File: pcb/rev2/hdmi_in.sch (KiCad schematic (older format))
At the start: 22 parts, among them CN1 MOLEX_500254-1927, IC8 PRTR5V0U2X, IC9 PRTR5V0U2X, Q1 BSS84LT1G, Q2 2N7002, Q3 2N7002, Q4 2N7002

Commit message: pcb wip
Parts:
- C1, C28: footprint CAPC1608X87N -> Capacitors SMD:CAPC1608X87N
- D10: footprint SOD3715X145N -> ICs And Semiconductors SMD:SOD3715X145N
- IC8, IC9: footprint SOT190P230X110-4N -> ICs And Semiconductors SMD:SOT190P230X110-4N
- Q1: footprint SOT95P240X110-3N -> ICs And Semiconductors SMD:SOT95P240X110-3N
- Q2, Q3, Q4: footprint SOT95P240X130-3N -> ICs And Semiconductors SMD:SOT95P240X130-3N
- R22, R23, R24, R25, R26, R27, R28, R29, R30, R31: footprint RESC1608X55N -> Resistors SMD:RESC1608X55N
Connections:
- wire segments 123 -> 98
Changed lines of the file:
@@
 F 0 "R27" V 1904 3510 50  0000 L CNN
 F 1 "R0603_1M_1%_0.1W_100PPM" H 1800 3240 60  0001 L CNN
-F 2 "RESC1608X55N" H 1800 2430 60  0001 L CNN
+F 2 "Resistors SMD:RESC1608X55N" H 1800 2430 60  0001 L CNN
 F 3 "\\cern.ch\\dfs\\Applications\\Altium\\Datasheets\\R0603_NIC_NRC.pdf" H 1800 3060 60  0001 L CNN
 F 4 "1M" V 1995 3510 50  0000 L CNN "~"
@@
 F 0 "C28" V 1504 3560 50  0000 L CNN
 F 1 "CC0603_100NF_50V_10%_X7R" H 1400 3190 60  0001 L CNN
-F 2 "CAPC1608X87N" H 1400 2380 60  0001 L CNN
+F 2 "Capacitors SMD:CAPC1608X87N" H 1400 2380 60  0001 L CNN
 F 3 "\\cern.ch\\dfs\\Applications\\Altium\\Datasheets\\CC0603_X7R_PHYCOMP.pdf" H 1400 3010 60  0001 L CNN
 F 4 "100nF" V 1595 3560 50  0000 L CNN "~"
@@
 F 0 "R30" V 1604 4610 50  0000 L CNN
 F 1 "R0603_3K3_1%_0.1W_100PPM" H 1500 4340 60  0001 L CNN
-F 2 "RESC1608X55N" H 1500 3530 60  0001 L CNN
+F 2 "Resistors SMD:RESC1608X55N" H 1500 3530 60  0001 L CNN
 F 3 "\\cern.ch\\dfs\\Applications\\Altium\\Datasheets\\R0603_NIC_NRC.pdf" H 1500 4160 60  0001 L CNN
 F 4 "3k3" V 1695 4610 50  0000 L CNN "~"
@@
 F 0 "R31" V 1604 5110 50  0000 L CNN
 F 1 "R0603_3K3_1%_0.1W_100PPM" H 1500 4840 60  0001 L CNN
-F 2 "RESC1608X55N" H 1500 4030 60  0001 L CNN
+F 2 "Resistors SMD:RESC1608X55N" H 1500 4030 60  0001 L CNN
 F 3 "\\cern.ch\\dfs\\Applications\\Altium\\Datasheets\\R0603_NIC_NRC.pdf" H 1500 4660 60  0001 L CNN
 F 4 "3k3" V 1695 5110 50  0000 L CNN "~"
@@
 F 0 "IC8" H 4550 4985 50  0000 C CNN
 F 1 "PRTR5V0U2X" H 4550 5076 50  0000 C CNN
-F 2 "SOT190P230X110-4N" H 4350 4060 60  0001 L CNN
+F 2 "ICs And Semiconductors SMD:SOT190P230X110-4N" H 4350 4060 60  0001 L CNN
 F 3 "\\cern.ch\\dfs\\Applications\\Altium\\Datasheets\\PRTR5V0U2X.pdf" H 4350 4780 60  0001 L CNN
 F 4 "PRTR5V0U2X" H 4350 4690 60  0001 L CNN "Part Number"
@@
 F 0 "IC9" H 4550 5835 50  0000 C CNN
 F 1 "PRTR5V0U2X" H 4550 5926 50  0000 C CNN
-F 2 "SOT190P230X110-4N" H 4350 4910 60  0001 L CNN
+F 2 "ICs And Semiconductors SMD:SOT190P230X110-4N" H 4350 4910 60  0001 L CNN
 F 3 "\\cern.ch\\dfs\\Applications\\Altium\\Datasheets\\PRTR5V0U2X.pdf" H 4350 5630 60  0001 L CNN
 F 4 "PRTR5V0U2X" H 4350 5540 60  0001 L CNN "Part Number"
@@
 F 0 "C1" V 2604 3560 50  0000 L CNN
 F 1 "CC0603_100NF_50V_10%_X7R" H 2500 3190 60  0001 L CNN
-F 2 "CAPC1608X87N" H 2500 2380 60  0001 L CNN
+F 2 "Capacitors SMD:CAPC1608X87N" H 2500 2380 60  0001 L CNN
 F 3 "\\cern.ch\\dfs\\Applications\\Altium\\Datasheets\\CC0603_X7R_PHYCOMP.pdf" H 2500 3010 60  0001 L CNN
 F 4 "100nF" V 2695 3560 50  0000 L CNN "~"
@@
 F 0 "Q3" V 4300 3500 50  0000 C CNN
 F 1 "2N7002" V 4400 3450 50  0000 C CNN
-F 2 "SOT95P240X130-3N" H 4550 2040 60  0001 L CNN
+F 2 "ICs And Semiconductors SMD:SOT95P240X130-3N" H 4550 2040 60  0001 L CNN
 F 3 "\\cern.ch\\dfs\\Applications\\Altium\\Datasheets\\2N7002.pdf" H 4550 2760 60  0001 L CNN
 F 4 "Value" H 4550 3250 60  0001 C CNN "Fieldname"
@@
 F 0 "Q4" V 4914 4150 50  0000 C CNN
 F 1 "2N7002" V 5005 4150 50  0000 C CNN
-F 2 "SOT95P240X130-3N" H 4550 2890 60  0001 L CNN
+F 2 "ICs And Semiconductors SMD:SOT95P240X130-3N" H 4550 2890 60  0001 L CNN
 F 3 "\\cern.ch\\dfs\\Applications\\Altium\\Datasheets\\2N7002.pdf" H 4550 3610 60  0001 L CNN
 F 4 "Value" H 4550 4100 60  0001 C CNN "Fieldname"
@@
 F 0 "R24" V 4204 3160 50  0000 L CNN
 F 1 "R0603_3K3_1%_0.1W_100PPM" H 4100 2890 60  0001 L CNN
-F 2 "RESC1608X55N" H 4100 2080 60  0001 L CNN
+F 2 "Resistors SMD:RESC1608X55N" H 4100 2080 60  0001 L CNN
 F 3 "\\cern.ch\\dfs\\Applications\\Altium\\Datasheets\\R0603_NIC_NRC.pdf" H 4100 2710 60  0001 L CNN
 F 4 "3k3" V 4295 3160 50  0000 L CNN "~"
@@
 F 0 "R25" V 4954 3160 50  0000 L CNN
 F 1 "R0603_3K3_1%_0.1W_100PPM" H 4850 2890 60  0001 L CNN
-F 2 "RESC1608X55N" H 4850 2080 60  0001 L CNN
+F 2 "Resistors SMD:RESC1608X55N" H 4850 2080 60  0001 L CNN
 F 3 "\\cern.ch\\dfs\\Applications\\Altium\\Datasheets\\R0603_NIC_NRC.pdf" H 4850 2710 60  0001 L CNN
 F 4 "3k3" V 5045 3160 50  0000 L CNN "~"
@@
 F 0 "R29" V 4954 4010 50  0000 L CNN
 F 1 "R0603_3K3_1%_0.1W_100PPM" H 4850 3740 60  0001 L CNN
-F 2 "RESC1608X55N" H 4850 2930 60  0001 L CNN
+F 2 "Resistors SMD:RESC1608X55N" H 4850 2930 60  0001 L CNN
 F 3 "\\cern.ch\\dfs\\Applications\\Altium\\Datasheets\\R0603_NIC_NRC.pdf" H 4850 3560 60  0001 L CNN
 F 4 "3k3" V 5045 4010 50  0000 L CNN "~"
@@
 F 0 "R28" V 3854 3960 50  0000 L CNN
 F 1 "R0603_3K3_1%_0.1W_100PPM" H 3750 3690 60  0001 L CNN
-F 2 "RESC1608X55N" H 3750 2880 60  0001 L CNN
+F 2 "Resistors SMD:RESC1608X55N" H 3750 2880 60  0001 L CNN
 F 3 "\\cern.ch\\dfs\\Applications\\Altium\\Datasheets\\R0603_NIC_NRC.pdf" H 3750 3510 60  0001 L CNN
 F 4 "3k3" V 3945 3960 50  0000 L CNN "~"
@@
 	1700 1050 2100 1050
 Wire Wire Line
-	2100 1050 2100 1350
-Wire Wire Line
-	2100 1350 2100 1650
-Wire Wire Line
-	2100 1650 2100 1950
-Wire Wire Line
-	2100 1950 2100 2550
-Wire Wire Line
-	2100 2550 2100 3900
+	2100 1050 2100 3900
 Wire Wire Line
 	1700 1350 2100 1350
@@
 Connection ~ 2100 2550
 Wire Wire Line
-	2100 3900 1800 3900
-Wire Wire Line
-	1800 3900 1400 3900
+	2100 3900 1400 3900
 Wire Wire Line
 	1400 3900 1400 3750
 Wire Wire Line
-	1800 3750 1800 3900
-Wire Wire Line
-	1800 3900 1800 4100
+	1800 3750 1800 4100
 Connection ~ 1800 3900
 Wire Wire Line
@@
 	1400 3300 1800 3300
 Wire Wire Line
-	1800 2950 1800 3300
-Wire Wire Line
-	1800 3300 1800 3450
+	1800 2950 1800 3450
 Wire Wire Line
 	1800 2950 1700 2950
@@
 	1700 2450 3300 2450
 Wire Wire Line
-	1700 2650 2850 2650
-Wire Wire Line
-	2850 2650 3750 2650
-Wire Wire Line
-	3750 2650 4100 2650
-Wire Wire Line
-	4100 2650 6050 2650
-Wire Wire Line
-	6050 2650 6500 2650
+	1700 2650 6500 2650
 Wire Wire Line
 	1700 2750 5350 2750
 Wire Wire Line
-	2850 2650 2850 3300
-Wire Wire Line
-	2850 3300 2850 4450
-Wire Wire Line
-	2850 4450 2850 5550
-Wire Wire Line
-	2850 5550 2850 6400
+	2850 2650 2850 6400
 Wire Wire Line
 	2850 4450 1500 4450
@@
 	1500 4450 1500 4550
 Wire Wire Line
-	1500 4850 1500 4900
-Wire Wire Line
-	1500 4900 1500 5050
+	1500 4850 1500 5050
 Wire Wire Line
 	1500 5450 1500 5350
@@
 	2500 4100 2500 3750
 Wire Wire Line
-	4550 2950 4550 3000
-Wire Wire Line
-	4550 3000 4550 3250
+	4550 2950 4550 3250
 Wire Wire Line
 	4550 3000 4850 3000
@@
 Connection ~ 4550 3000
 Wire Wire Line
-	4550 3850 4550 3900
-Wire Wire Line
-	4550 3900 4550 4100
+	4550 3850 4550 4100
 Wire Wire Line
 	4550 3900 4850 3900
@@
 Connection ~ 4550 3900
 Wire Wire Line
-	4700 4350 4850 4350
-Wire Wire Line
-	4850 4350 5050 4350
+	4700 4350 5050 4350
 Wire Wire Line
 	4850 4350 4850 4250
 Connection ~ 4850 4350
 Wire Wire Line
-	4700 3500 4850 3500
-Wire Wire Line
-	4850 3500 5050 3500
+	4700 3500 5050 3500
 Wire Wire Line
 	4850 3500 4850 3400
 Connection ~ 4850 3500
 Wire Wire Line
-	3400 3500 4100 3500
-Wire Wire Line
-	4100 3500 4300 3500
+	3400 3500 4300 3500
 Wire Wire Line
 	4100 3500 4100 3400
 Wire Wire Line
-	3300 4350 3750 4350
-Wire Wire Line
-	3750 4350 4300 4350
+	3300 4350 4300 4350
 Wire Wire Line
 	3750 4350 3750 4200
@@
 F 0 "Q1" H 6620 2904 50  0000 L CNN
 F 1 "BSS84LT1G" H 6620 2995 50  0000 L CNN
-F 2 "SOT95P240X110-3N" H 6300 1690 60  0001 L CNN
+F 2 "ICs And Semiconductors SMD:SOT95P240X110-3N" H 6300 1690 60  0001 L CNN
 F 3 "\\cern.ch\\dfs\\Applications\\Altium\\Datasheets\\BSS84LT1G.pdf" H 6300 2410 60  0001 L CNN
 F 4 "BSS84LT1G" H 6300 2320 60  0001 L CNN "Part Number"
@@
 F 0 "R23" H 5800 3145 50  0000 C CNN
 F 1 "R0603_1K_1%_0.1W_100PPM" H 5650 3040 60  0001 L CNN
-F 2 "RESC1608X55N" H 5650 2230 60  0001 L CNN
+F 2 "Resistors SMD:RESC1608X55N" H 5650 2230 60  0001 L CNN
 F 3 "\\cern.ch\\dfs\\Applications\\Altium\\Datasheets\\R0603_NIC_NRC.pdf" H 5650 2860 60  0001 L CNN
 F 4 "1k" H 5800 3054 50  0000 C CNN "~"
@@
 	5950 3250 6050 3250
 Wire Wire Line
-	6050 3150 6050 3250
-Wire Wire Line
-	6050 3250 6050 3450
+	6050 3150 6050 3450
 Connection ~ 4100 2650
 Wire Wire Line
@@
 F 0 "R22" V 6604 2760 50  0000 L CNN
 F 1 "R0603_3K3_1%_0.1W_100PPM" H 6500 2490 60  0001 L CNN
-F 2 "RESC1608X55N" H 6500 1680 60  0001 L CNN
+F 2 "Resistors SMD:RESC1608X55N" H 6500 1680 60  0001 L CNN
 F 3 "\\cern.ch\\dfs\\Applications\\Altium\\Datasheets\\R0603_NIC_NRC.pdf" H 6500 2310 60  0001 L CNN
 F 4 "3k3" V 6695 2760 50  0000 L CNN "~"
@@
 F 0 "Q2" H 6620 3796 50  0000 L CNN
 F 1 "2N7002" H 6620 3705 50  0000 L CNN
-F 2 "SOT95P240X130-3N" H 6300 2490 60  0001 L CNN
+F 2 "ICs And Semiconductors SMD:SOT95P240X130-3N" H 6300 2490 60  0001 L CNN
 F 3 "\\cern.ch\\dfs\\Applications\\Altium\\Datasheets\\2N7002.pdf" H 6300 3210 60  0001 L CNN
 F 4 "2N7002" H 6300 3120 60  0001 L CNN "Part Number"
@@
 F 0 "R26" V 6554 3810 50  0000 L CNN
 F 1 "R0603_3K3_1%_0.1W_100PPM" H 6450 3540 60  0001 L CNN
-F 2 "RESC1608X55N" H 6450 2730 60  0001 L CNN
+F 2 "Resistors SMD:RESC1608X55N" H 6450 2730 60  0001 L CNN
 F 3 "\\cern.ch\\dfs\\Applications\\Altium\\Datasheets\\R0603_NIC_NRC.pdf" H 6450 3360 60  0001 L CNN
 F 4 "3k3" V 6645 3810 50  0000 L CNN "~"
@@
 $EndComp
 Wire Wire Line
-	6300 3700 6450 3700
-Wire Wire Line
-	6450 3700 7050 3700
+	6300 3700 7050 3700
 Wire Wire Line
 	6450 3700 6450 3750
@@
 	7100 5850 7000 5850
 Wire Wire Line
-	7000 5850 7000 5950
-Wire Wire Line
-	7000 5950 7000 6050
+	7000 5850 7000 6050
 Wire Wire Line
 	7000 5950 7100 5950
@@
 	9300 5850 9200 5850
 Wire Wire Line
-	9200 5850 9200 5950
-Wire Wire Line
-	9200 5950 9200 6050
+	9200 5850 9200 6050
 Wire Wire Line
 	9200 5950 9300 5950
@@
 F 0 "D10" H 6800 4573 50  0000 C CNN
 F 1 "BAS170" H 6800 4664 50  0000 C CNN
-F 2 "SOD3715X145N" H 6650 4320 60  0001 L CNN
+F 2 "ICs And Semiconductors SMD:SOD3715X145N" H 6650 4320 60  0001 L CNN
 F 3 "\\cern.ch\\dfs\\Applications\\Altium\\Datasheets\\MBR0530PBF.pdf" H 6650 4230 60  0001 L CNN
 F 4 "Value" H 6650 4800 60  0001 C CNN "Fieldname"

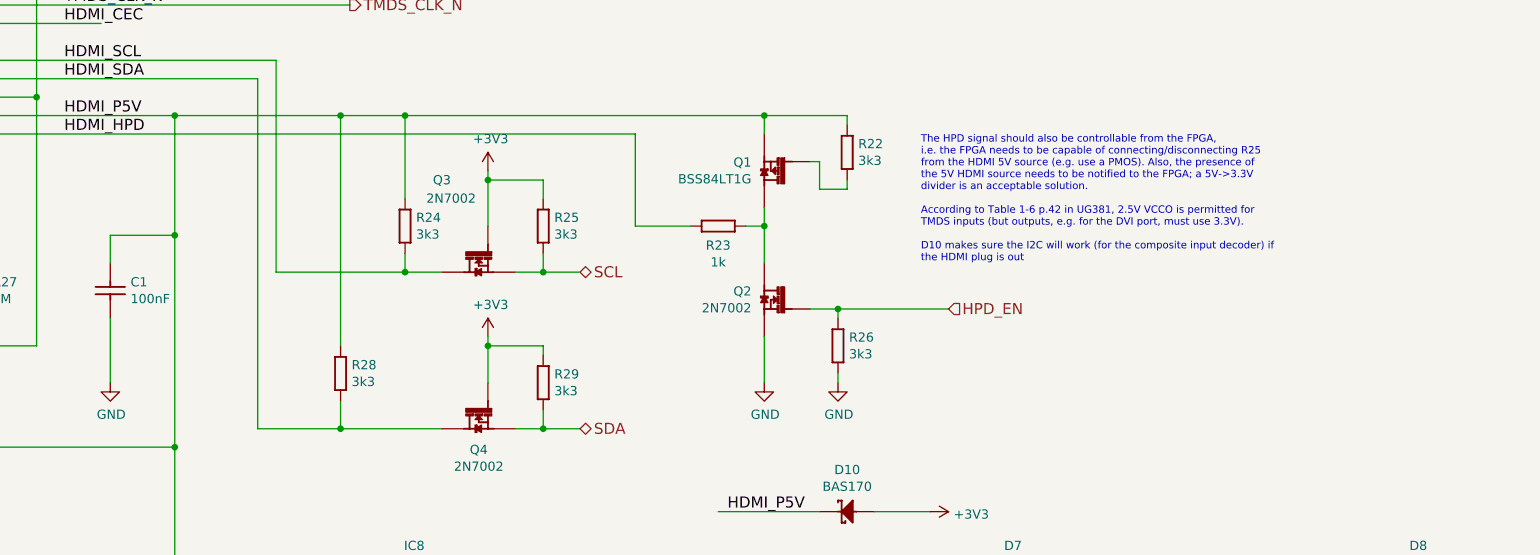
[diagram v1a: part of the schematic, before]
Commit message: Completed port to KiCad, passes DRC+LVS. NOT MANUFACTURED.
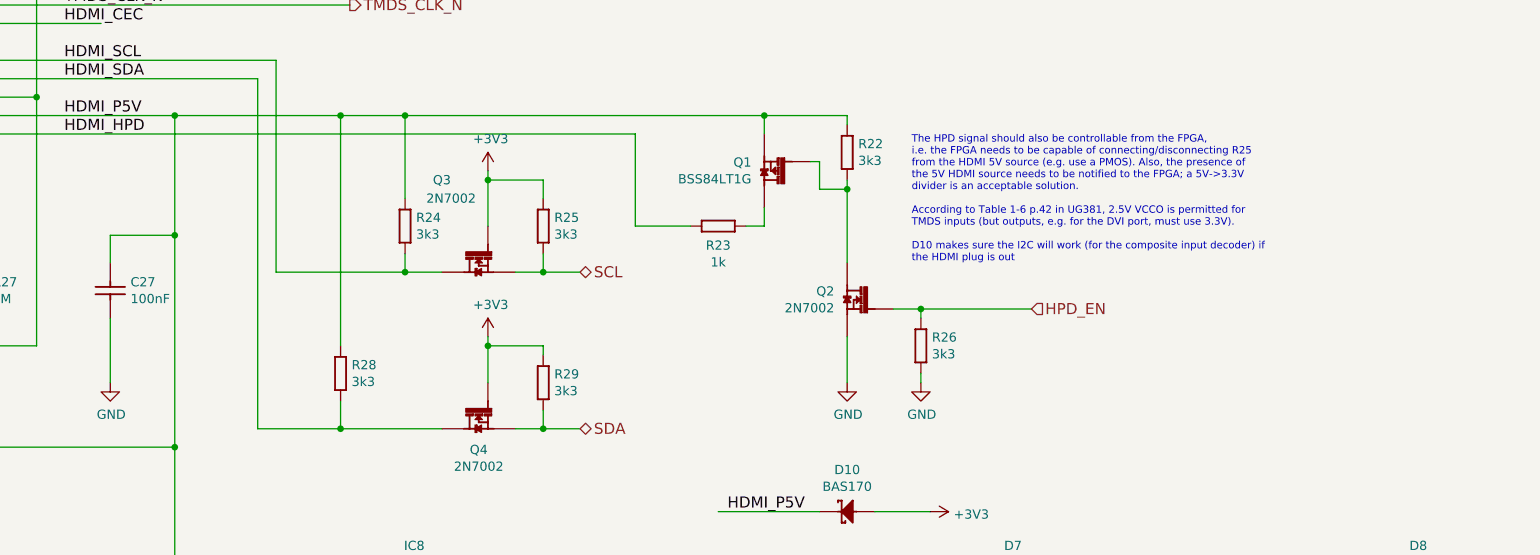
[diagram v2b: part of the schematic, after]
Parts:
- D10: footprint ICs And Semiconductors SMD:SOD3715X145N -> ICs And Semiconductors SMD:SOD2713X115N
- D7, D8: footprint (none) -> dsi_shield:SOT1176-1; Fieldname (none) -> Value
- renumbered C1 to C27
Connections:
- wire segments 98 -> 99
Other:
- moved on the sheet: Q2, R26

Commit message: axi4/zynq version: wip
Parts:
- C27, C28: symbol CC0603_100NF_50V_10%_X7R -> dsi_shield-rescue:CC0603_100NF_50V_10%_X7R-
- CN1: symbol MOLEX_500254-1927 -> dsi_shield-rescue:MOLEX_500254-1927-
- D10: symbol Diode_Schottky -> dsi_shield-rescue:Diode_Schottky-
- D7, D8: symbol IP4292CZ10 -> dsi_shield-rescue:IP4292CZ10-
- IC8, IC9: symbol PRTR5V0U2X -> dsi_shield-rescue:PRTR5V0U2X-
- Q1: symbol BSS84LT1G -> dsi_shield-rescue:BSS84LT1G-
- Q2, Q3, Q4: symbol 2N7002 -> dsi_shield-rescue:2N7002-
- R22, R24, R25, R26, R28, R29, R30, R31: symbol R0603_3K3_1%_0.1W_100PPM -> dsi_shield-rescue:R0603_3K3_1%_0.1W_100PPM-
- R23: symbol R0603_1K_1%_0.1W_100PPM -> dsi_shield-rescue:R0603_1K_1%_0.1W_100PPM-
- R27: symbol R0603_1M_1%_0.1W_100PPM -> dsi_shield-rescue:R0603_1M_1%_0.1W_100PPM-
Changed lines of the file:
@@
-EESchema Schematic File Version 2
-LIBS:Capacitors Networks THD
-LIBS:Capacitors Networks SMD
-LIBS:Capacitors THD
-LIBS:Capacitors SMD
-LIBS:Miscellaneous
-LIBS:HARWIN
-LIBS:LEMO
-LIBS:WEIDMULLER
-LIBS:FCI
-LIBS:MOLEX
-LIBS:TYCO
-LIBS:ERNI
-LIBS:MENTOR
-LIBS:SAMTEC
-LIBS:STELVIO-KONTEK COMATEL
-LIBS:AMPHENOL
-LIBS:HARTING
-LIBS:3M
-LIBS:Pads
-LIBS:Switches
-LIBS:Relays
-LIBS:Heat-Sinks
-LIBS:Fasteners & Fixings
-LIBS:Batteries
-LIBS:Fuses
-LIBS:Metal Screening Box
-LIBS:Sockets
-LIBS:Regulators
-LIBS:Transistors
-LIBS:Power Supplies
-LIBS:Analog & Interface
-LIBS:Sensors
-LIBS:Logic
-LIBS:Optocouplers
-LIBS:Standard Logic
-LIBS:DC-DC Converters
-LIBS:Operational Amplifiers
-LIBS:Crystals & Oscillators
-LIBS:Diodes
-LIBS:LEDs & Displays
-LIBS:PCB Modules
-LIBS:Bonding
-LIBS:Resistors THD
-LIBS:Potentiometers SMD
-LIBS:Thermistors And Varistors
-LIBS:Potentiometers THD
-LIBS:Resistor Networks THD
-LIBS:Resistors SMD
-LIBS:Resistor Networks SMD
-LIBS:Transformers
-LIBS:Inductors SMD
-LIBS:Inductors THD
-LIBS:Cores
-LIBS:power
-LIBS:conn
-LIBS:dsi_shield
+EESchema Schematic File Version 4
 LIBS:dsi_shield-cache
 EELAYER 26 0
@@
 $EndDescr
 $Comp
-L MOLEX_500254-1927 J?
+L dsi_shield-rescue:MOLEX_500254-1927- J?
 U 1 1 59999F77
 P 1500 750
@@
 $EndComp
 $Comp
-L R0603_1M_1%_0.1W_100PPM R?
+L dsi_shield-rescue:R0603_1M_1%_0.1W_100PPM- R?
 U 1 1 59999FAE
 P 1800 3450
@@
 $EndComp
 $Comp
-L CC0603_100NF_50V_10%_X7R C?
+L dsi_shield-rescue:CC0603_100NF_50V_10%_X7R- C?
 U 1 1 59999FDA
 P 1400 3450
@@
 $EndComp
 $Comp
-L GND #PWR039
+L dsi_shield-rescue:GND- #PWR039
 U 1 1 59999FEA
 P 1800 4100
@@
 HDMI_CEC
 $Comp
-L R0603_3K3_1%_0.1W_100PPM R30
+L dsi_shield-rescue:R0603_3K3_1%_0.1W_100PPM- R30
 U 1 1 5999AB0C
 P 1500 4550
@@
 $EndComp
 $Comp
-L R0603_3K3_1%_0.1W_100PPM R31
+L dsi_shield-rescue:R0603_3K3_1%_0.1W_100PPM- R31
 U 1 1 5999AC5E
 P 1500 5050
@@
 $EndComp
 $Comp
-L GND #PWR040
+L dsi_shield-rescue:GND- #PWR040
 U 1 1 5999ACD8
 P 1500 5450
@@
 HPD_NOTIF
 $Comp
-L PRTR5V0U2X IC8
+L dsi_shield-rescue:PRTR5V0U2X- IC8
 U 1 1 5999C2A3
 P 4350 5650
@@
 $EndComp
 $Comp
-L PRTR5V0U2X IC9
+L dsi_shield-rescue:PRTR5V0U2X- IC9
 U 1 1 5999C42E
 P 4350 6500
@@
 HDMI_SDA
 $Comp
-L GND #PWR041
+L dsi_shield-rescue:GND- #PWR041
 U 1 1 5999C6B4
 P 4650 5550
@@
 $EndComp
 $Comp
-L GND #PWR042
+L dsi_shield-rescue:GND- #PWR042
 U 1 1 5999C727
 P 4650 6400
@@
 HDMI_HPD
 $Comp
-L CC0603_100NF_50V_10%_X7R C?
+L dsi_shield-rescue:CC0603_100NF_50V_10%_X7R- C?
 U 1 1 5999D084
 P 2500 3450
@@
 $EndComp
 $Comp
-L GND #PWR043
+L dsi_shield-rescue:GND- #PWR043
 U 1 1 5999D19C
 P 2500 4100
@@
 $EndComp
 $Comp
-L 2N7002 Q3
+L dsi_shield-rescue:2N7002- Q3
 U 1 1 5999E138
 P 4550 3250
@@
 $EndComp
 $Comp
-L 2N7002 Q4
+L dsi_shield-rescue:2N7002- Q4
 U 1 1 5999ED55
 P 4550 4100
@@
 $EndComp
 $Comp
-L R0603_3K3_1%_0.1W_100PPM R24
+L dsi_shield-rescue:R0603_3K3_1%_0.1W_100PPM- R24
 U 1 1 599A03F7
 P 4100 3100
@@
 $EndComp
 $Comp
-L R0603_3K3_1%_0.1W_100PPM R25
+L dsi_shield-rescue:R0603_3K3_1%_0.1W_100PPM- R25
 U 1 1 599A05E7
 P 4850 3100
@@
 $EndComp
 $Comp
-L R0603_3K3_1%_0.1W_100PPM R29
+L dsi_shield-rescue:R0603_3K3_1%_0.1W_100PPM- R29
 U 1 1 599A0684
 P 4850 3950
@@
 $EndComp
 $Comp
-L R0603_3K3_1%_0.1W_100PPM R28
+L dsi_shield-rescue:R0603_3K3_1%_0.1W_100PPM- R28
 U 1 1 599A0727
 P 3750 3900
@@
 $EndComp
 $Comp
-L +3V3 #PWR044
+L dsi_shield-rescue:+3V3- #PWR044
 U 1 1 599A09BE
 P 4550 2950
@@
 $EndComp
 $Comp
-L +3V3 #PWR045
+L dsi_shield-rescue:+3V3- #PWR045
 U 1 1 599A0AEB
 P 4550 3850
@@
 	5350 2750 5350 3250
 $Comp
-L BSS84LT1G Q1
+L dsi_shield-rescue:BSS84LT1G- Q1
 U 1 1 599A6CE3
 P 6300 2900
@@
 $EndComp
 $Comp
-L R0603_1K_1%_0.1W_100PPM R23
+L dsi_shield-rescue:R0603_1K_1%_0.1W_100PPM- R23
 U 1 1 599A8E93
 P 5650 3250
@@
 	6050 2650 6050 2750
 $Comp
-L R0603_3K3_1%_0.1W_100PPM R22
+L dsi_shield-rescue:R0603_3K3_1%_0.1W_100PPM- R22
 U 1 1 599A9D4C
 P 6500 2700
@@
 	6350 2900 6300 2900
 $Comp
-L 2N7002 Q2
+L dsi_shield-rescue:2N7002- Q2
 U 1 1 599AA988
 P 6750 3700
@@
 $EndComp
 $Comp
-L GND #PWR046
+L dsi_shield-rescue:GND- #PWR046
 U 1 1 599AABDA
 P 6500 4100
@@
 $EndComp
 $Comp
-L R0603_3K3_1%_0.1W_100PPM R26
+L dsi_shield-rescue:R0603_3K3_1%_0.1W_100PPM- R26
 U 1 1 599AAC36
 P 6900 3750
@@
 	6900 3700 6900 3750
 $Comp
-L GND #PWR047
+L dsi_shield-rescue:GND- #PWR047
 U 1 1 599AADCE
 P 6900 4100
@@
 	6650 4800 6950 4800
 $Comp
-L +3V3 #PWR048
+L dsi_shield-rescue:+3V3- #PWR048
 U 1 1 599AE1C6
 P 6950 4800
@@
 $EndComp
 $Comp
-L IP4292CZ10 D7
+L dsi_shield-rescue:IP4292CZ10- D7
 U 1 1 599AEDEC
 P 7200 3950
@@
 TMDS_CLK_N
 $Comp
-L IP4292CZ10 D8
+L dsi_shield-rescue:IP4292CZ10- D8
 U 1 1 599B2763
 P 9400 3950
@@
 Connection ~ 7000 5950
 $Comp
-L GND #PWR049
+L dsi_shield-rescue:GND- #PWR049
 U 1 1 599B50BC
 P 7000 6050
@@
 Connection ~ 9200 5950
 $Comp
-L GND #PWR050
+L dsi_shield-rescue:GND- #PWR050
 U 1 1 599B66EC
 P 9200 6050
@@
 	3150 6850 750  6850
 $Comp
-L Diode_Schottky D10
+L dsi_shield-rescue:Diode_Schottky- D10
 U 1 1 59908931
 P 6650 4800
